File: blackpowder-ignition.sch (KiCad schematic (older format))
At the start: 6 parts, among them J8 Conn_01x02, U1 TCA9555PWR

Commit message: everything hooked up, cleaned layout up, silkscreen
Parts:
- added J1: CAS_stacking, star-common-lib:CAS_physical, symbol star-common-lib:CAS_stacking
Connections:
- net +3V3: now also J1.A35 (3.3VA), J1.A36 (3.3VB)
- net GND: now also J1.A37 (GND10), J1.A38 (GND11)
- net CAS_bus/I2C0_SCL renamed SCL
- net SCL: now also J1.A13 (I2C0_SCL)
- net CAS_bus/I2C0_SDA renamed SDA
- net SDA: now also J1.A14 (I2C0_SDA)
- no-connect marks 9 -> 83
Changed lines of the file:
@@
 $Descr A4 11693 8268
 encoding utf-8
-Sheet 1 6
+Sheet 1 5
 Title ""
 Date ""
@@
 F2 "ignite" I L 3550 2400 50
 F3 "~cont~" I L 3550 2550 50
-$EndSheet
-$Sheet
-S 600  1200 550  300
-U 5ED2D9A2
-F0 "CAS_bus" 39
-F1 "hardware-sch-blocks/CAS_bus/CAS_bus.sch" 20
-F2 "I2C0_SCL" I R 1150 1400 50
-F3 "I2C0_SDA" I R 1150 1300 50
 $EndSheet
 NoConn ~ 1450 1500
@@
 NoConn ~ 2850 2200
 NoConn ~ 2850 2300
+$Comp
+L star-common-lib:CAS_stacking J1
+U 1 1 5EF8309E
+P 1800 6150
+F 0 "J1" H 1800 7367 50  0000 C CNN
+F 1 "CAS_stacking" H 1800 7276 50  0000 C CNN
+F 2 "star-common-lib:CAS_physical" H 1900 7100 50  0001 C CNN
+F 3 "" H 1900 7100 50  0001 C CNN
+	1    1800 6150
+	1    0    0    -1
+$EndComp
+NoConn ~ 4400 7100
+NoConn ~ 4400 7000
+NoConn ~ 4400 6900
+NoConn ~ 4400 6800
+NoConn ~ 4400 6700
+NoConn ~ 4400 6600
+NoConn ~ 4400 6500
+NoConn ~ 4400 6400
+NoConn ~ 4400 6300
+NoConn ~ 4400 6200
+NoConn ~ 4400 6100
+NoConn ~ 4400 6000
+NoConn ~ 4400 5900
+NoConn ~ 4400 5800
+NoConn ~ 4400 5700
+NoConn ~ 4400 5600
+NoConn ~ 4400 5500
+NoConn ~ 4400 5400
+NoConn ~ 4400 5300
+NoConn ~ 4400 5200
+NoConn ~ 3000 7100
+NoConn ~ 3000 7000
+NoConn ~ 3000 6900
+NoConn ~ 3000 6800
+NoConn ~ 3000 6700
+NoConn ~ 3000 6600
+NoConn ~ 3000 6500
+NoConn ~ 3000 6400
+NoConn ~ 3000 6300
+NoConn ~ 3000 6200
+NoConn ~ 3000 6100
+NoConn ~ 3000 6000
+NoConn ~ 3000 5900
+NoConn ~ 3000 5800
+NoConn ~ 3000 5700
+NoConn ~ 3000 5600
+NoConn ~ 3000 5500
+NoConn ~ 3000 5400
+NoConn ~ 3000 5300
+NoConn ~ 3000 5200
+NoConn ~ 2500 7100
+NoConn ~ 2500 6800
+NoConn ~ 2500 6700
+NoConn ~ 2500 6600
+NoConn ~ 2500 6500
+NoConn ~ 2500 6400
+NoConn ~ 2500 6300
+NoConn ~ 2500 6200
+NoConn ~ 2500 6100
+NoConn ~ 2500 6000
+NoConn ~ 2500 5900
+NoConn ~ 2500 5700
+NoConn ~ 2500 5600
+NoConn ~ 2500 5500
+NoConn ~ 2500 5400
+NoConn ~ 2500 5300
+NoConn ~ 2500 5200
+NoConn ~ 1100 5200
+NoConn ~ 1100 5300
+NoConn ~ 1100 5400
+NoConn ~ 1100 5500
+NoConn ~ 1100 5600
+NoConn ~ 1100 5700
+NoConn ~ 1100 6100
+NoConn ~ 1100 6200
+NoConn ~ 1100 6300
+NoConn ~ 1100 6400
+NoConn ~ 1100 6500
+NoConn ~ 1100 6600
+NoConn ~ 1100 6700
+NoConn ~ 1100 6800
+NoConn ~ 1100 7100
+$Comp
+L power:+3.3V #PWR0125
+U 1 1 5EFA22B2
+P 850 6900
+F 0 "#PWR0125" H 850 6750 50  0001 C CNN
+F 1 "+3.3V" H 865 7073 50  0000 C CNN
+F 2 "" H 850 6900 50  0001 C CNN
+F 3 "" H 850 6900 50  0001 C CNN
+	1    850  6900
+	1    0    0    -1
+$EndComp
+$Comp
+L power:GND #PWR0126
+U 1 1 5EFA5DEC
+P 850 7000
+F 0 "#PWR0126" H 850 6750 50  0001 C CNN
+F 1 "GND" H 855 6827 50  0000 C CNN
+F 2 "" H 850 7000 50  0001 C CNN
+F 3 "" H 850 7000 50  0001 C CNN
+	1    850  7000
+	1    0    0    -1
+$EndComp
+Wire Wire Line
+	850  7000 1100 7000
+Wire Wire Line
+	1100 6900 850  6900
+NoConn ~ 1100 5900
+Wire Wire Line
+	800  5800 1100 5800
+NoConn ~ 1100 6000
+Text Label 800  5800 0    50   ~ 0
+SCL
+$Comp
+L star-common-lib:CAS_stacking J1
+U 2 1 5EF84BE0
+P 3700 6150
+F 0 "J1" H 3700 7367 50  0000 C CNN
+F 1 "CAS_stacking" H 3700 7276 50  0000 C CNN
+F 2 "star-common-lib:CAS_physical" H 3800 7100 50  0001 C CNN
+F 3 "" H 3800 7100 50  0001 C CNN
+	2    3700 6150
+	1    0    0    -1
+$EndComp
+Wire Wire Line
+	2800 5800 2500 5800
+Text Label 2800 5800 2    50   ~ 0
+SDA
+Text Label 1150 1400 0    50   ~ 0
+SCL
+Text Label 1150 1300 0    50   ~ 0
+SDA
+$Comp
+L power:+3.3V #PWR05
+U 1 1 5F005042
+P 2700 6900
+F 0 "#PWR05" H 2700 6750 50  0001 C CNN
+F 1 "+3.3V" H 2715 7073 50  0000 C CNN
+F 2 "" H 2700 6900 50  0001 C CNN
+F 3 "" H 2700 6900 50  0001 C CNN
+	1    2700 6900
+	1    0    0    -1
+$EndComp
+$Comp
+L power:GND #PWR06
+U 1 1 5F00685B
+P 2700 7000
+F 0 "#PWR06" H 2700 6750 50  0001 C CNN
+F 1 "GND" H 2705 6827 50  0000 C CNN
+F 2 "" H 2700 7000 50  0001 C CNN
+F 3 "" H 2700 7000 50  0001 C CNN
+	1    2700 7000
+	1    0    0    -1
+$EndComp
+Wire Wire Line
+	2500 6900 2700 6900
+Wire Wire Line
+	2500 7000 2700 7000
+$Comp
+L power:PWR_FLAG #FLG0101
+U 1 1 5EFD7138
+P 5300 3950
+F 0 "#FLG0101" H 5300 4025 50  0001 C CNN
+F 1 "PWR_FLAG" H 5300 4123 50  0000 C CNN
+F 2 "" H 5300 3950 50  0001 C CNN
+F 3 "~" H 5300 3950 50  0001 C CNN
+	1    5300 3950
+	-1   0    0    1
+$EndComp
+$Comp
+L power:PWR_FLAG #FLG0102
+U 1 1 5EFD782F
+P 5700 3800
+F 0 "#FLG0102" H 5700 3875 50  0001 C CNN
+F 1 "PWR_FLAG" H 5700 3973 50  0000 C CNN
+F 2 "" H 5700 3800 50  0001 C CNN
+F 3 "~" H 5700 3800 50  0001 C CNN
+	1    5700 3800
+	1    0    0    -1
+$EndComp
+$Comp
+L power:GND #PWR0127
+U 1 1 5EFD7C86
+P 5700 3800
+F 0 "#PWR0127" H 5700 3550 50  0001 C CNN
+F 1 "GND" H 5705 3627 50  0000 C CNN
+F 2 "" H 5700 3800 50  0001 C CNN
+F 3 "" H 5700 3800 50  0001 C CNN
+	1    5700 3800
+	1    0    0    -1
+$EndComp
+$Comp
+L power:+BATT #PWR0128
+U 1 1 5EFD816F
+P 5300 3950
+F 0 "#PWR0128" H 5300 3800 50  0001 C CNN
+F 1 "+BATT" H 5315 4123 50  0000 C CNN
+F 2 "" H 5300 3950 50  0001 C CNN
+F 3 "" H 5300 3950 50  0001 C CNN
+	1    5300 3950
+	1    0    0    -1
+$EndComp
+$Comp
+L power:PWR_FLAG #FLG0103
+U 1 1 5EFDC2FD
+P 6050 3950
+F 0 "#FLG0103" H 6050 4025 50  0001 C CNN
+F 1 "PWR_FLAG" H 6050 4123 50  0000 C CNN
+F 2 "" H 6050 3950 50  0001 C CNN
+F 3 "~" H 6050 3950 50  0001 C CNN
+	1    6050 3950
+	-1   0    0    1
+$EndComp
+$Comp
+L power:+3.3V #PWR0129
+U 1 1 5EFDD50C
+P 6050 3950
+F 0 "#PWR0129" H 6050 3800 50  0001 C CNN
+F 1 "+3.3V" H 6065 4123 50  0000 C CNN
+F 2 "" H 6050 3950 50  0001 C CNN
+F 3 "" H 6050 3950 50  0001 C CNN
+	1    6050 3950
+	1    0    0    -1
+$EndComp
 $EndSCHEMATC

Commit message: most functionality
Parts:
- removed U1: TCA9555PWR, Package_SO:TSSOP-24_4.4x7.8mm_P0.65mm, symbol Interface_Expansion:TCA9555PWR
- added TP1, TP2, TP3, TP4, TP5, TP6, TP7, TP8: TestPoint, star-common-lib:TestPoint_Keystone_5117_Miniature, symbol Connector:TestPoint
- added TP10, TP11, TP9: TestPoint, star-common-lib:TestPoint_Keystone_5000_Miniature, symbol Connector:TestPoint
- added U1: TCA9534, Package_SO:TSSOP-16_4.4x5mm_P0.65mm, symbol Interface_Expansion:TCA9534
- J8: footprint Connector_Molex:Molex_Mini-Fit_Jr_5569-02A2_2x01_P4.20mm_Horizontal -> star-common-lib:Molex_Mini-Fit_Jr_5569-02A2_2x01_P4.20mm_Horizontal
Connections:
- net +3V3: now also TP11.1, U1.16 (VDD)
- net +BATT: now also TP9.1
- net A0: now also U1.1 (A0)
- net A1: now also U1.2 (A1)
- net A2: now also U1.3 (A2)
- net GND: now also TP10.1, U1.8 (GND)
- net SCL: now also U1.14 (SCL)
- net SDA: now also U1.15 (SDA)
- net igniteA: now also TP1.1, U1.4 (P0)
- net igniteB: now also TP2.1, U1.6 (P2)
- net igniteC: now also TP3.1, U1.9 (P4)
- net igniteD: now also TP4.1, U1.11 (P6)
- net ~contA~: now also TP5.1, U1.5 (P1)
- net ~contB~: now also TP6.1, U1.7 (P3)
- net ~contC~: now also TP7.1, U1.10 (P5)
- net ~contD~: now also TP8.1, U1.12 (P7)
- no-connect marks 83 -> 75
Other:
- note added: "CAS Bus"
- moved on the sheet: C1, J1A, J1B, J8, JP1, JP2, JP3

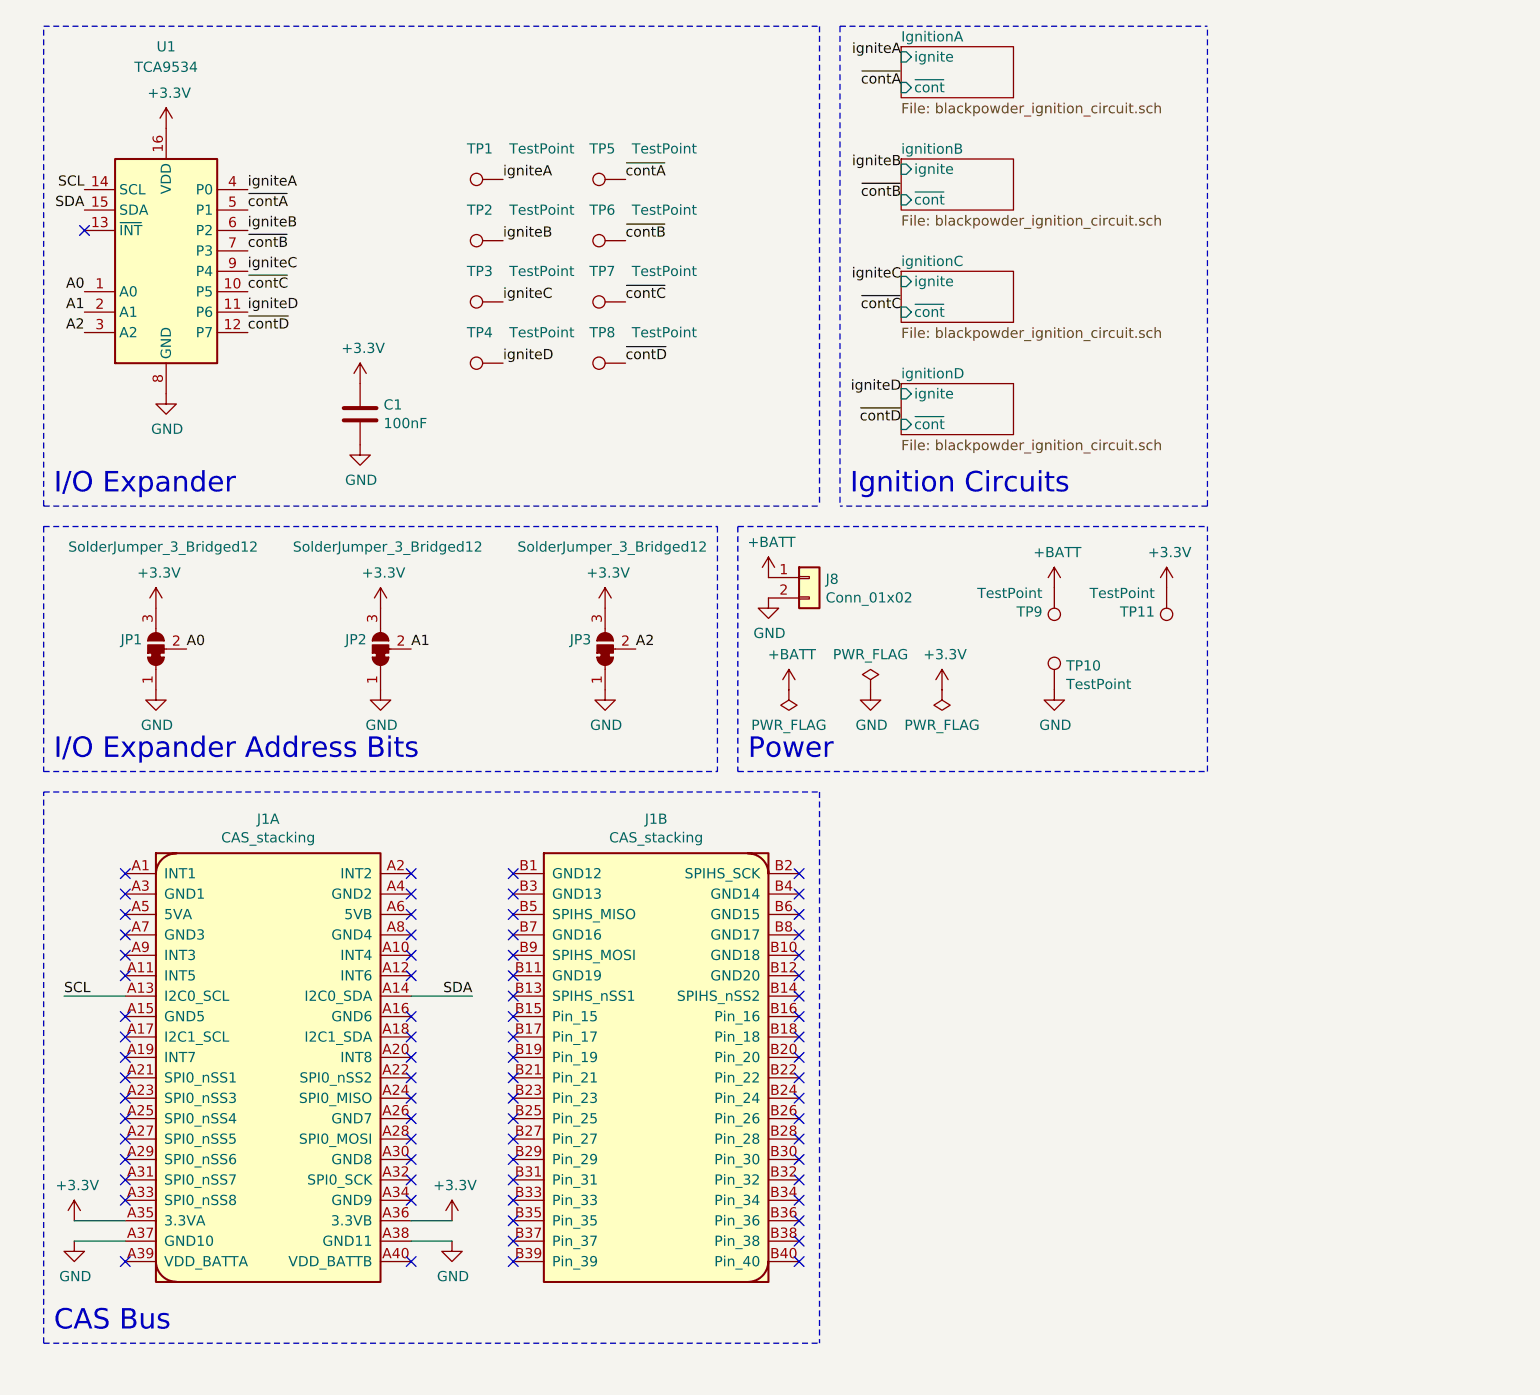
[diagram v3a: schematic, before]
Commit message: 8 charges on a module
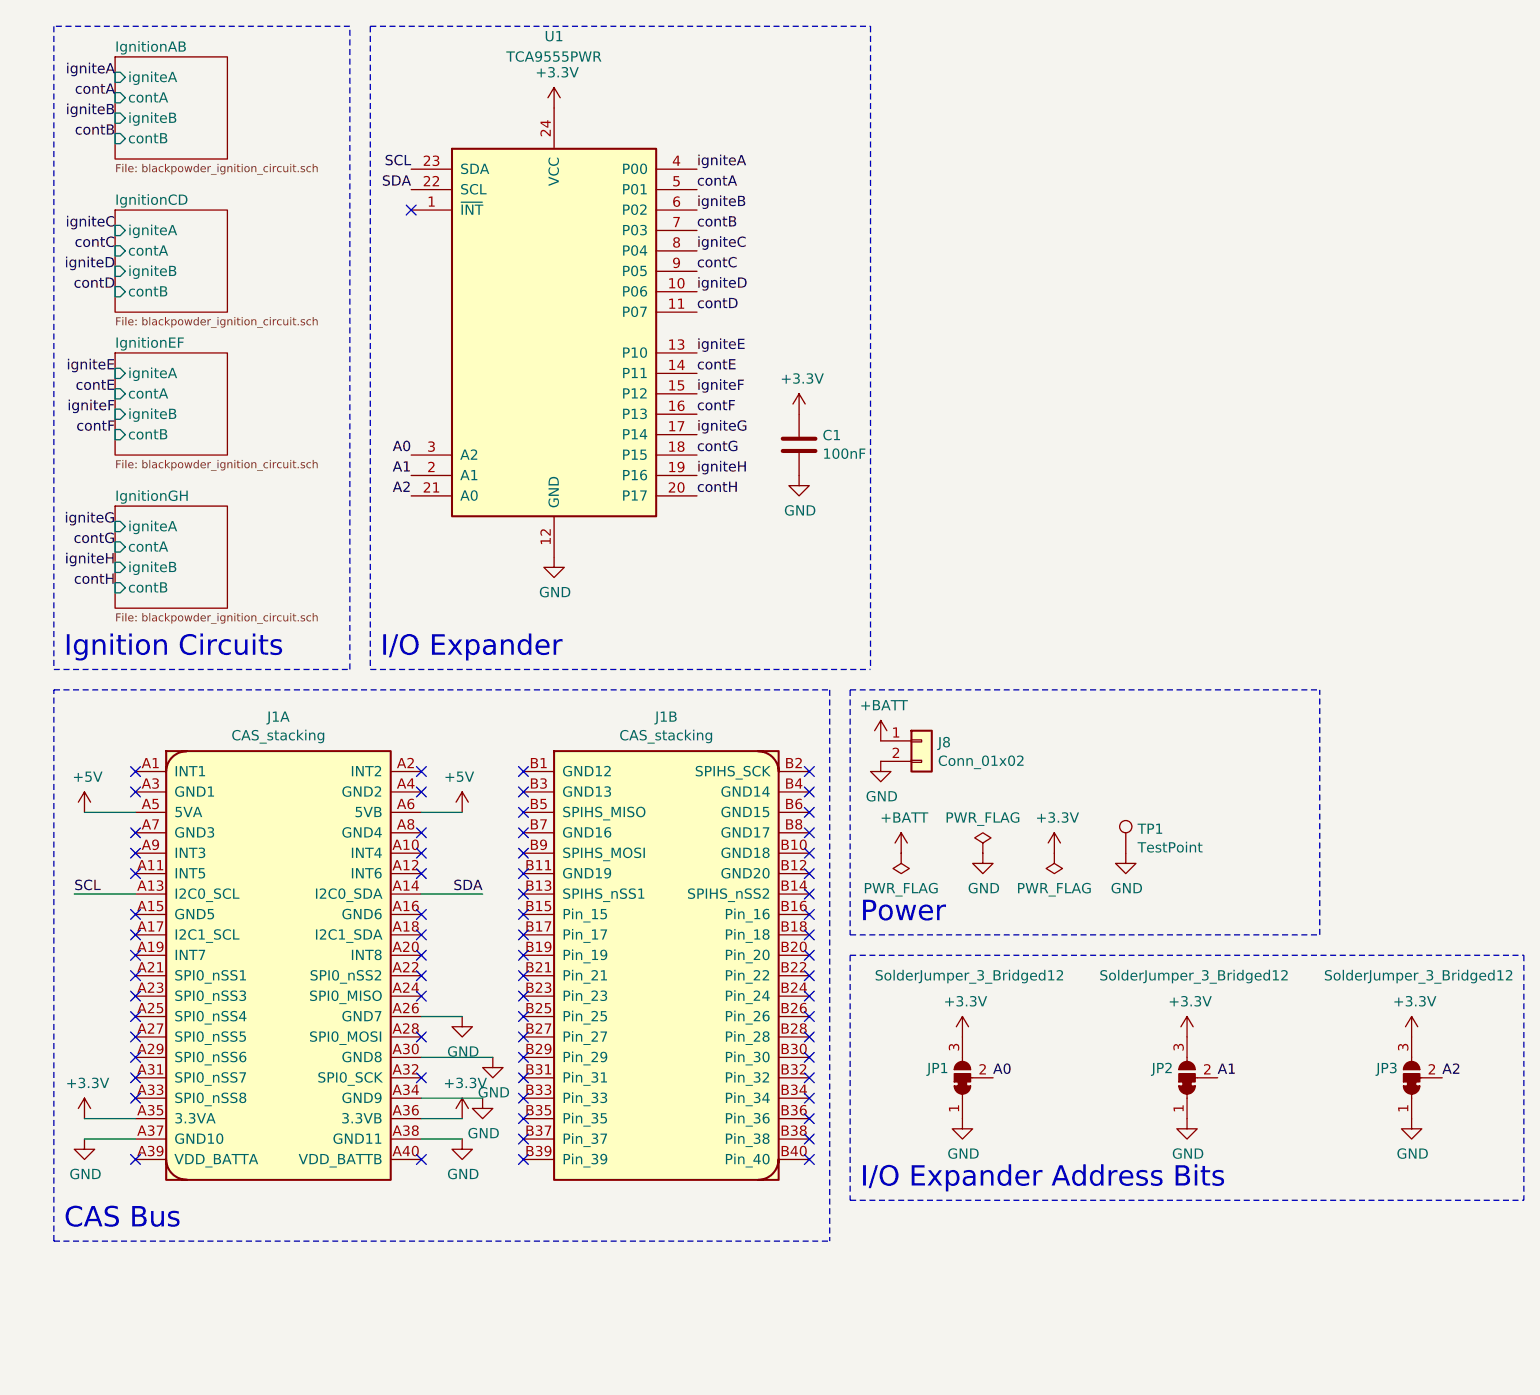
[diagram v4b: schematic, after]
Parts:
- removed TP10, TP11, TP9: TestPoint, star-common-lib:TestPoint_Keystone_5000_Miniature, symbol Connector:TestPoint
- removed TP2, TP3, TP4, TP5, TP6, TP7, TP8: TestPoint, star-common-lib:TestPoint_Keystone_5117_Miniature, symbol Connector:TestPoint
- removed U1: TCA9534, Package_SO:TSSOP-16_4.4x5mm_P0.65mm, symbol Interface_Expansion:TCA9534
- added U1: TCA9555PWR, Package_SO:TSSOP-24_4.4x7.8mm_P0.65mm, symbol Interface_Expansion:TCA9555PWR
- C1: footprint Capacitor_SMD:C_0603_1608Metric_Pad1.05x0.95mm_HandSolder -> Capacitor_SMD:C_0603_1608Metric_Pad1.08x0.95mm_HandSolder
- TP1: footprint star-common-lib:TestPoint_Keystone_5117_Miniature -> TestPoint:TestPoint_Keystone_5000-5004_Miniature
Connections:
- net +3V3: now also U1.24 (VCC)
- net A0: now also U1.3 (A2)
- net A1: now also U1.2 (A1)
- net A2: now also U1.21 (A0)
- net GND: now also J1.A26 (GND7), J1.A30 (GND8), J1.A34 (GND9), TP1.1, U1.12 (GND)
- net SCL: now also U1.23 (SDA)
- net SDA: now also U1.22 (SCL)
- net igniteA: now also U1.4 (P00); no longer TP1.1
- net igniteB: now also U1.6 (P02)
- net igniteC: now also U1.8 (P04)
- net igniteD: now also U1.10 (P06)
- net +5V: now reaches J1.A5 (5VA)
- net +5V: now also J1.A6 (5VB)
- new net contA: U1.5 (P01)
- new net contB: U1.7 (P03)
- new net contC: U1.9 (P05)
- new net contD: U1.11 (P07)
- new net contE: U1.14 (P11)
- new net contF: U1.16 (P13)
- new net contG: U1.18 (P15)
- new net contH: U1.20 (P17)
- new net igniteE: U1.13 (P10)
- new net igniteF: U1.15 (P12)
- new net igniteG: U1.17 (P14)
- new net igniteH: U1.19 (P16)
- no-connect marks 75 -> 70
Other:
- moved on the sheet: C1, J1A, J1B, J8, JP1, JP2, JP3
